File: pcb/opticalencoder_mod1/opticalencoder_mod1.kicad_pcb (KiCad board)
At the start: 2 copper layers, 65 x 25 mm, 26 parts, among them J1 Conn_Port, Q1 MMBT3904, Q2 MMBT3906, Q3 MMBT3906

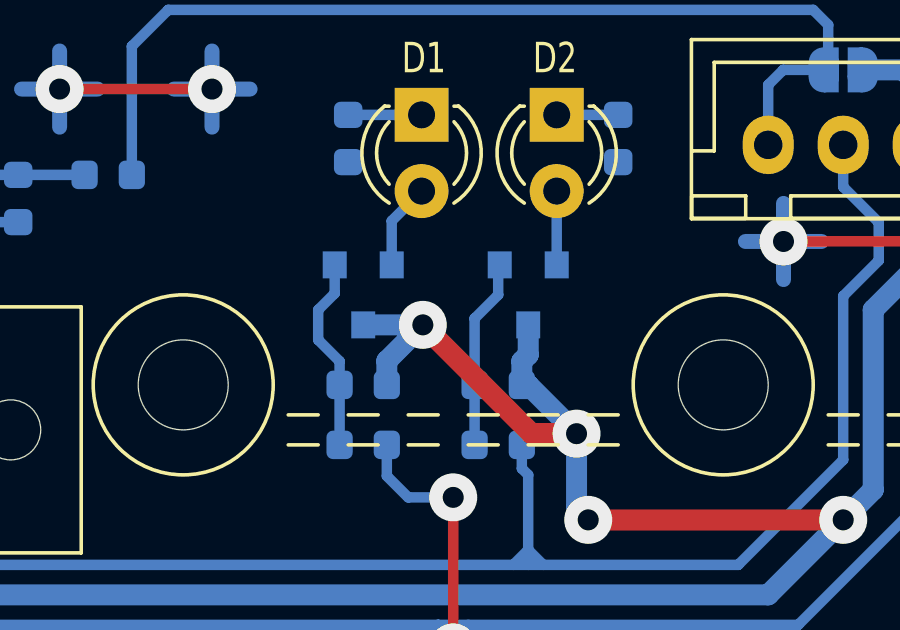
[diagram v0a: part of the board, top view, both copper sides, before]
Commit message: minor fix, B & E inverted on Q2 & Q3
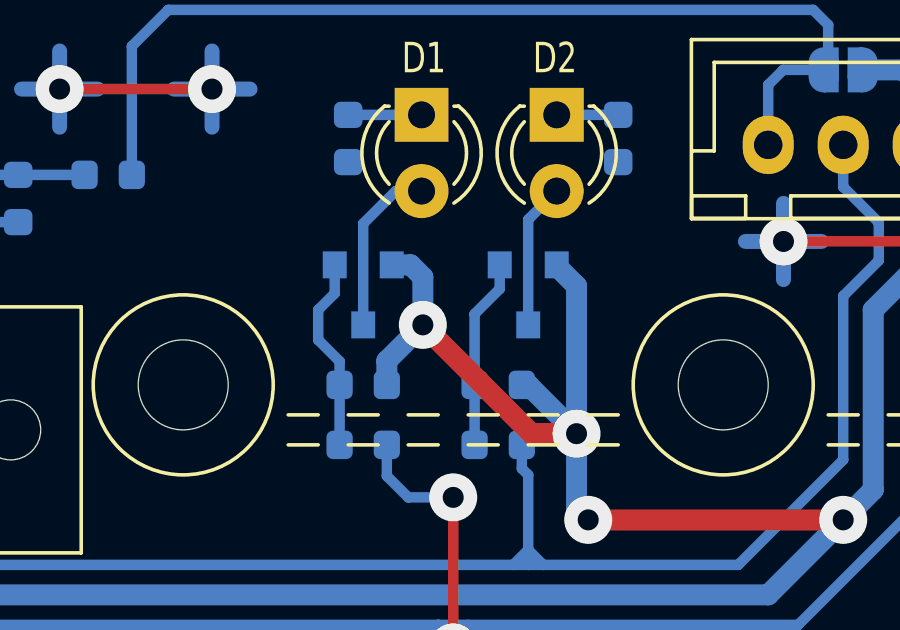
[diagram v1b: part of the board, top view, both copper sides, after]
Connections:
- Q2 pad 2: Net-(D1-Pad2) -> +3V3
- Q2 pad 3: +3V3 -> Net-(D1-Pad2)
- Q3 pad 2: Net-(D2-Pad2) -> +3V3
- Q3 pad 3: +3V3 -> Net-(D2-Pad2)
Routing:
- net +3V3: track 87.4 -> 92.0 mm
- net Net-(D1-Pad2): track 2.87 -> 5.77 mm
- net Net-(D2-Pad2): track 2.46 -> 4.85 mm
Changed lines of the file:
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@@
     (thickness 1.6)
     (drawings 57)
-    (tracks 129)
+    (tracks 133)
     (zones 0)
     (modules 26)
@@
   (title_block
     (title "Optical Encoder Prototype Board")
+    (date 2020-04-07)
     (rev 0.1)
     (company "codeA, C.A.")
@@
       (net 12 "Net-(Q2-Pad1)"))
     (pad 2 smd rect (at -1 -0.95 270) (size 0.9 0.8) (layers B.Cu B.Paste B.Mask)
+      (net 1 +3V3))
+    (pad 3 smd rect (at 1 0 270) (size 0.9 0.8) (layers B.Cu B.Paste B.Mask)
       (net 3 "Net-(D1-Pad2)"))
-    (pad 3 smd rect (at 1 0 270) (size 0.9 0.8) (layers B.Cu B.Paste B.Mask)
-      (net 1 +3V3))
     (model ${KISYS3DMOD}/Package_TO_SOT_SMD.3dshapes/SOT-23.wrl
       (at (xyz 0 0 0))
@@
     )
     (pad 3 smd rect (at 1 0 270) (size 0.9 0.8) (layers B.Cu B.Paste B.Mask)
+      (net 6 "Net-(D2-Pad2)"))
+    (pad 2 smd rect (at -1 -0.95 270) (size 0.9 0.8) (layers B.Cu B.Paste B.Mask)
       (net 1 +3V3))
-    (pad 2 smd rect (at -1 -0.95 270) (size 0.9 0.8) (layers B.Cu B.Paste B.Mask)
-      (net 6 "Net-(D2-Pad2)"))
     (pad 1 smd rect (at -1 0.95 270) (size 0.9 0.8) (layers B.Cu B.Paste B.Mask)
       (net 13 "Net-(Q3-Pad1)"))
@@
   (segment (start 112 116.5) (end 114 114.5) (width 0.7) (layer B.Cu) (net 1))
   (segment (start 112 118) (end 112 116.5) (width 0.7) (layer B.Cu) (net 1))
-  (segment (start 135 113) (end 135 112) (width 0.7) (layer B.Cu) (net 1))
-  (segment (start 134.7875 113.2125) (end 135 113) (width 0.7) (layer B.Cu) (net 1))
-  (segment (start 134.7875 114) (end 134.7875 113.2125) (width 0.7) (layer B.Cu) (net 1))
   (via (at 131.48748 112) (size 1.6) (drill 0.7) (layers F.Cu B.Cu) (net 1))
   (segment (start 135.114427 115.626947) (end 136.611203 115.626947) (width 0.7) (layer F.Cu) (net 1))
@@
   (segment (start 130.2875 113.19998) (end 131.48748 112) (width 0.7) (layer B.Cu) (net 1))
   (segment (start 130.2875 114) (end 130.2875 113.19998) (width 0.7) (layer B.Cu) (net 1))
-  (segment (start 129.5 112) (end 131.48748 112) (width 0.7) (layer B.Cu) (net 1))
   (segment (start 136.611203 115.611203) (end 136.611203 115.626947) (width 0.7) (layer B.Cu) (net 1))
   (segment (start 135 114) (end 136.611203 115.611203) (width 0.7) (layer B.Cu) (net 1))
@@
   (via (at 145.5 118.5) (size 1.6) (drill 0.7) (layers F.Cu B.Cu) (net 1))
   (segment (start 148 110) (end 148 106) (width 0.7) (layer B.Cu) (net 1))
+  (segment (start 135.95 110) (end 135.95 110.042) (width 0.7) (layer B.Cu) (net 1))
+  (segment (start 136.611203 110.703203) (end 136.611203 115.626947) (width 0.7) (layer B.Cu) (net 1))
+  (segment (start 135.95 110.042) (end 136.611203 110.703203) (width 0.7) (layer B.Cu) (net 1))
+  (segment (start 130.45 110) (end 131.082 110) (width 0.7) (layer B.Cu) (net 1))
+  (segment (start 131.48748 110.40548) (end 131.48748 112) (width 0.7) (layer B.Cu) (net 1))
+  (segment (start 131.082 110) (end 131.48748 110.40548) (width 0.7) (layer B.Cu) (net 1))
   (via (at 124.46 104.14) (size 1.6) (drill 0.7) (layers F.Cu B.Cu) (net 2))
   (segment (start 124.46 104.14) (end 119.38 104.14) (width 0.35) (layer F.Cu) (net 2))
@@
   (segment (start 143.51 109.22) (end 142.24 109.22) (width 0.5) (layer B.Cu) (net 2))
   (segment (start 143.51 109.22) (end 143.51 107.95) (width 0.5) (layer B.Cu) (net 2))
-  (segment (start 130.45 108.535) (end 131.445 107.54) (width 0.35) (layer B.Cu) (net 3))
-  (segment (start 130.45 110) (end 130.45 108.535) (width 0.35) (layer B.Cu) (net 3))
+  (segment (start 130.585 107.54) (end 131.445 107.54) (width 0.35) (layer B.Cu) (net 3))
+  (segment (start 129.5 108.625) (end 130.585 107.54) (width 0.35) (layer B.Cu) (net 3))
+  (segment (start 129.5 112) (end 129.5 108.625) (width 0.35) (layer B.Cu) (net 3))
   (segment (start 129 105) (end 131.445 105) (width 0.35) (layer B.Cu) (net 4))
   (segment (start 138 105) (end 135.95 105) (width 0.35) (layer B.Cu) (net 5))
-  (segment (start 135.95 110) (end 135.95 107.54) (width 0.35) (layer B.Cu) (net 6))
+  (segment (start 135 108.49) (end 135.95 107.54) (width 0.35) (layer B.Cu) (net 6))
+  (segment (start 135 112) (end 135 108.49) (width 0.35) (layer B.Cu) (net 6))
   (segment (start 110 119.5) (end 112.5 122) (width 0.35) (layer B.Cu) (net 7))
   (segment (start 110 118) (end 110 119.5) (width 0.35) (layer B.Cu) (net 7))
@@
   (segment (start 114 108) (end 112.2125 108) (width 0.35) (layer B.Cu) (net 11))
   (segment (start 128.7125 116) (end 128.7125 114) (width 0.35) (layer B.Cu) (net 12))
-  (segment (start 128.55 110.95) (end 128.55 110) (width 0.35) (layer B.Cu) (net 12))
-  (segment (start 128 111.5) (end 128.55 110.95) (width 0.35) (layer B.Cu) (net 12))
   (segment (start 128 112.5) (end 128 111.5) (width 0.35) (layer B.Cu) (net 12))
   (segment (start 128.7125 113.2125) (end 128 112.5) (width 0.35) (layer B.Cu) (net 12))
   (segment (start 128.7125 114) (end 128.7125 113.2125) (width 0.35) (layer B.Cu) (net 12))
+  (segment (start 128.55 110.95) (end 128 111.5) (width 0.35) (layer B.Cu) (net 12))
+  (segment (start 128.55 110) (end 128.55 110.95) (width 0.35) (layer B.Cu) (net 12))
   (segment (start 133.2125 116) (end 133.2125 114) (width 0.35) (layer B.Cu) (net 13))
   (segment (start 134 110.05) (end 134.05 110) (width 0.35) (layer B.Cu) (net 13))
-  (segment (start 134 111) (end 134 110.05) (width 0.35) (layer B.Cu) (net 13))
-  (segment (start 133.2125 111.7875) (end 134 111) (width 0.35) (layer B.Cu) (net 13))
-  (segment (start 133.2125 114) (end 133.2125 111.7875) (width 0.35) (layer B.Cu) (net 13))
+  (segment (start 134.05 110.8) (end 134.05 110) (width 0.35) (layer B.Cu) (net 13))
+  (segment (start 133.2125 111.6375) (end 134.05 110.8) (width 0.35) (layer B.Cu) (net 13))
+  (segment (start 133.2125 114) (end 133.2125 111.6375) (width 0.35) (layer B.Cu) (net 13))
   (segment (start 112 113) (end 112 109.7875) (width 0.35) (layer B.Cu) (net 14))
   (zone (net 2) (net_name GND) (layer B.Cu) (hatch edge 0.508)
